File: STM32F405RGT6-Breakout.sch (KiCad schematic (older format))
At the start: 1 part

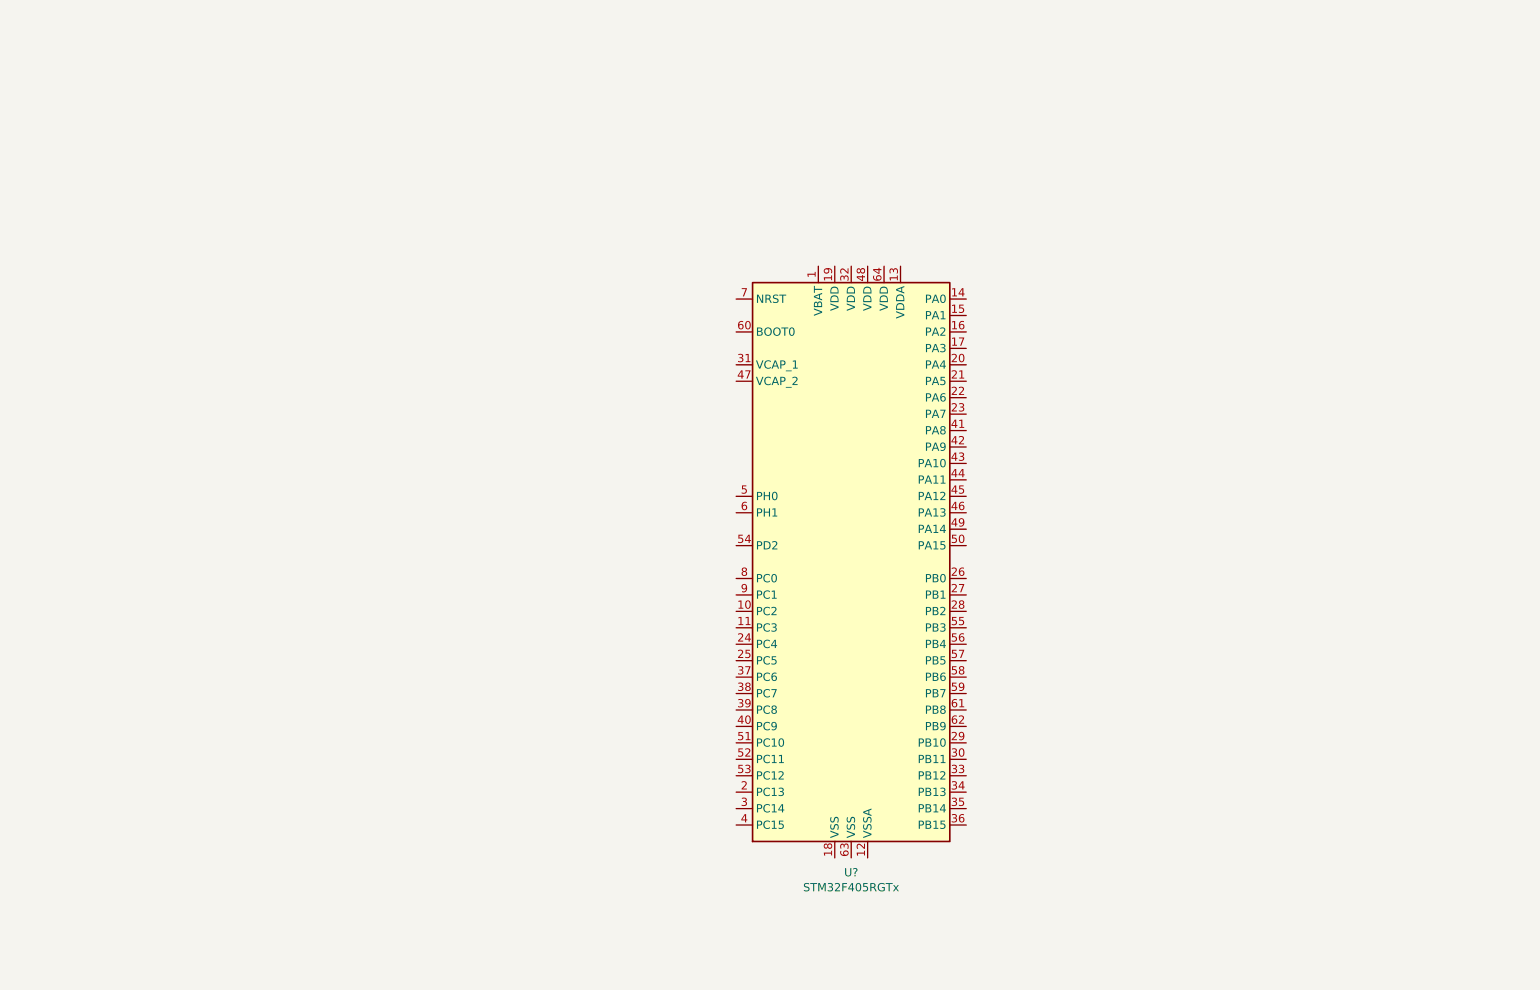
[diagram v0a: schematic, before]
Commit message: Input voltage regulator with pch input reverse polarity protection
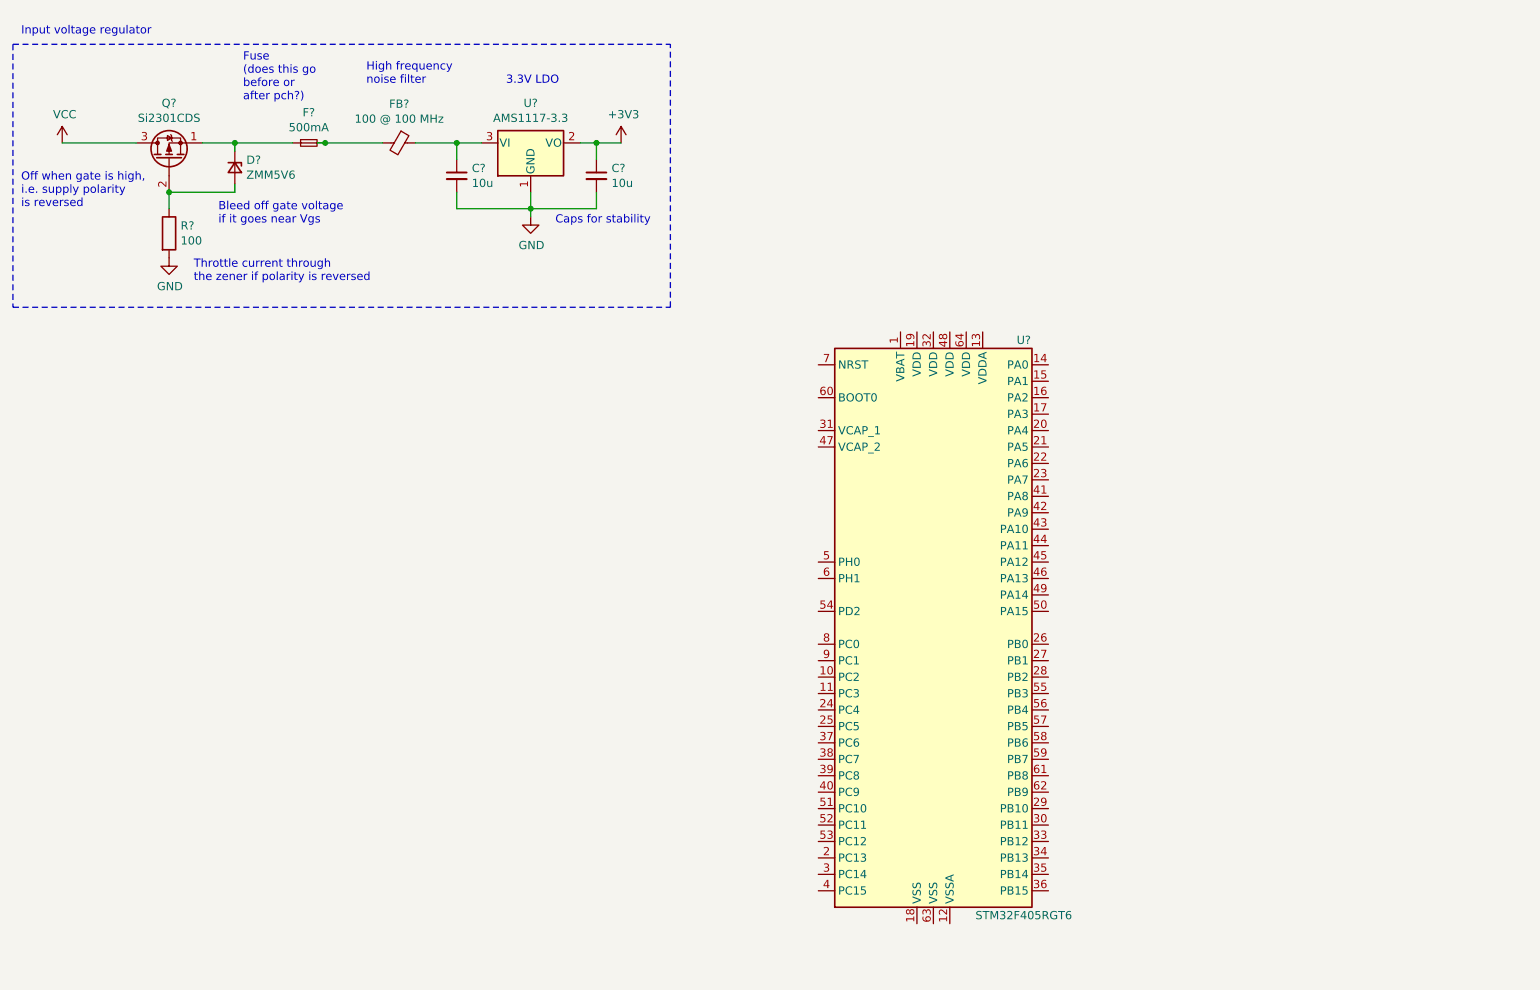
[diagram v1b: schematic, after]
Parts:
- added C? (x2): 10u, symbol Device:C_Small
- added D?: ZMM5V6, symbol Device:D_Zener_Small
- added F?: 500mA, symbol Device:Fuse_Small
- added FB?: 100 @ 100 MHz, symbol Device:Ferrite_Bead_Small
- added Q?: Si2301CDS, symbol Device:Q_PMOS_SGD
- added R?: 100, symbol Device:R
- added U?: AMS1117-3.3, Package_TO_SOT_SMD:SOT-223-3_TabPin2, symbol Regulator_Linear:AMS1117-3.3
- U?: value STM32F405RGTx -> STM32F405RGT6
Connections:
- net labels added: +3V3, GND, VCC
- wire segments 0 -> 21
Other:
- note added: "3.3V LDO"
- note added: "Bleed off gate voltage \nif it goes near Vgs"
- note added: "Caps for stability\n"
- note added: "Fuse\n(does this go \nbefore or \nafter pch?)"
- note added: "High frequency \nnoise filter\n"
- note added: "Input voltage regulator"
- note added: "Off when gate is high,\ni.e. supply polarity \nis reversed"
- note added: "Throttle current through\nthe zener if polarity is reversed\n"
- moved on the sheet: U?
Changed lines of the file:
@@
 L MCU_ST_STM32F4:STM32F405RGTx U?
 U 1 1 61902656
-P 5750 3900
-F 0 "U?" H 5750 2011 50  0000 C CNN
-F 1 "STM32F405RGTx" H 5750 1920 50  0000 C CNN
-F 2 "Package_QFP:LQFP-64_10x10mm_P0.5mm" H 5150 2200 50  0001 R CNN
-F 3 "http://www.st.com/st-web-ui/static/active/en/resource/technical/document/datasheet/DM00037051.pdf" H 5750 3900 50  0001 C CNN
-	1    5750 3900
-	1    0    0    -1
-$EndComp
+P 6250 4300
+F 0 "U?" H 6800 6050 50  0000 C CNN
+F 1 "STM32F405RGT6" H 6800 2550 50  0000 C CNN
+F 2 "Package_QFP:LQFP-64_10x10mm_P0.5mm" H 5650 2600 50  0001 R CNN
+F 3 "http://www.st.com/st-web-ui/static/active/en/resource/technical/document/datasheet/DM00037051.pdf" H 6250 4300 50  0001 C CNN
+	1    6250 4300
+	1    0    0    -1
+$EndComp
+$Comp
+L Regulator_Linear:AMS1117-3.3 U?
+U 1 1 6192F648
+P 3800 1350
+F 0 "U?" H 3800 1592 50  0000 C CNN
+F 1 "AMS1117-3.3" H 3800 1501 50  0000 C CNN
+F 2 "Package_TO_SOT_SMD:SOT-223-3_TabPin2" H 3800 1550 50  0001 C CNN
+F 3 "http://www.advanced-monolithic.com/pdf/ds1117.pdf" H 3900 1100 50  0001 C CNN
+	1    3800 1350
+	1    0    0    -1
+$EndComp
+$Comp
+L Device:Ferrite_Bead_Small FB?
+U 1 1 619351E4
+P 3000 1350
+F 0 "FB?" V 2763 1350 50  0000 C CNN
+F 1 "100 @ 100 MHz" V 2854 1350 50  0000 C CNN
+F 2 "" V 2930 1350 50  0001 C CNN
+F 3 "~" H 3000 1350 50  0001 C CNN
+	1    3000 1350
+	0    1    1    0
+$EndComp
+$Comp
+L Device:Fuse_Small F?
+U 1 1 61935A18
+P 2450 1350
+F 0 "F?" H 2450 1535 50  0000 C CNN
+F 1 "500mA" H 2450 1444 50  0000 C CNN
+F 2 "" H 2450 1350 50  0001 C CNN
+F 3 "~" H 2450 1350 50  0001 C CNN
+	1    2450 1350
+	1    0    0    -1
+$EndComp
+$Comp
+L Device:D_Zener_Small D?
+U 1 1 61943D90
+P 2000 1500
+F 0 "D?" V 1954 1570 50  0000 L CNN
+F 1 "ZMM5V6" V 2045 1570 50  0000 L CNN
+F 2 "" V 2000 1500 50  0001 C CNN
+F 3 "~" V 2000 1500 50  0001 C CNN
+	1    2000 1500
+	0    1    1    0
+$EndComp
+$Comp
+L Device:R R?
+U 1 1 61945077
+P 1600 1900
+F 0 "R?" H 1670 1946 50  0000 L CNN
+F 1 "100" H 1670 1855 50  0000 L CNN
+F 2 "" V 1530 1900 50  0001 C CNN
+F 3 "~" H 1600 1900 50  0001 C CNN
+	1    1600 1900
+	1    0    0    -1
+$EndComp
+Wire Wire Line
+	1600 1650 1600 1750
+Wire Wire Line
+	2000 1650 2000 1600
+Wire Wire Line
+	2000 1400 2000 1350
+Wire Wire Line
+	2500 1350 2550 1350
+Wire Wire Line
+	3100 1350 3350 1350
+$Comp
+L power:GND #PWR?
+U 1 1 6194D181
+P 1600 2050
+F 0 "#PWR?" H 1600 1800 50  0001 C CNN
+F 1 "GND" H 1605 1877 50  0000 C CNN
+F 2 "" H 1600 2050 50  0001 C CNN
+F 3 "" H 1600 2050 50  0001 C CNN
+	1    1600 2050
+	1    0    0    -1
+$EndComp
+$Comp
+L power:VCC #PWR?
+U 1 1 6195256A
+P 950 1350
+F 0 "#PWR?" H 950 1200 50  0001 C CNN
+F 1 "VCC" H 965 1523 50  0000 C CNN
+F 2 "" H 950 1350 50  0001 C CNN
+F 3 "" H 950 1350 50  0001 C CNN
+	1    950  1350
+	1    0    0    -1
+$EndComp
+Wire Wire Line
+	950  1350 1400 1350
+Text Notes 1750 2200 0    50   ~ 0
+Throttle current through\nthe zener if polarity is reversed\n
+Wire Wire Line
+	2000 1350 1800 1350
+Wire Wire Line
+	2000 1350 2350 1350
+Text Notes 1900 1850 0    50   ~ 0
+Bleed off gate voltage \nif it goes near Vgs
+Text Notes 700  1750 0    50   ~ 0
+Off when gate is high,\ni.e. supply polarity \nis reversed
+$Comp
+L power:GND #PWR?
+U 1 1 6194DC8B
+P 3800 1800
+F 0 "#PWR?" H 3800 1550 50  0001 C CNN
+F 1 "GND" H 3805 1627 50  0000 C CNN
+F 2 "" H 3800 1800 50  0001 C CNN
+F 3 "" H 3800 1800 50  0001 C CNN
+	1    3800 1800
+	1    0    0    -1
+$EndComp
+$Comp
+L Device:C_Small C?
+U 1 1 6195B580
+P 3350 1550
+F 0 "C?" H 3442 1596 50  0000 L CNN
+F 1 "10u" H 3442 1505 50  0000 L CNN
+F 2 "" H 3350 1550 50  0001 C CNN
+F 3 "~" H 3350 1550 50  0001 C CNN
+	1    3350 1550
+	1    0    0    -1
+$EndComp
+$Comp
+L Device:C_Small C?
+U 1 1 6195E545
+P 4200 1550
+F 0 "C?" H 4292 1596 50  0000 L CNN
+F 1 "10u" H 4292 1505 50  0000 L CNN
+F 2 "" H 4200 1550 50  0001 C CNN
+F 3 "~" H 4200 1550 50  0001 C CNN
+	1    4200 1550
+	1    0    0    -1
+$EndComp
+Connection ~ 3350 1350
+Wire Wire Line
+	3350 1350 3500 1350
+Wire Wire Line
+	3350 1750 3800 1750
+Wire Wire Line
+	4200 1750 4200 1650
+Connection ~ 3800 1750
+Wire Wire Line
+	3800 1750 4200 1750
+Wire Wire Line
+	3800 1750 3800 1800
+Wire Wire Line
+	4350 1350 4200 1350
+$Comp
+L power:+3V3 #PWR?
+U 1 1 61961ED5
+P 4350 1350
+F 0 "#PWR?" H 4350 1200 50  0001 C CNN
+F 1 "+3V3" H 4365 1523 50  0000 C CNN
+F 2 "" H 4350 1350 50  0001 C CNN
+F 3 "" H 4350 1350 50  0001 C CNN
+	1    4350 1350
+	1    0    0    -1
+$EndComp
+Connection ~ 4200 1350
+Wire Wire Line
+	4200 1350 4100 1350
+Connection ~ 2550 1350
+Wire Wire Line
+	2550 1350 2900 1350
+Text Notes 3950 1850 0    50   ~ 0
+Caps for stability\n
+Text Notes 2800 1000 0    50   ~ 0
+High frequency \nnoise filter\n
+Connection ~ 2000 1350
+$Comp
+L Device:Q_PMOS_SGD Q?
+U 1 1 61942650
+P 1600 1450
+F 0 "Q?" V 1942 1450 50  0000 C CNN
+F 1 "Si2301CDS" V 1851 1450 50  0000 C CNN
+F 2 "" H 1800 1550 50  0001 C CNN
+F 3 "~" H 1600 1450 50  0001 C CNN
+	1    1600 1450
+	0    -1   -1   0
+$EndComp
+Wire Wire Line
+	2000 1650 1600 1650
+Connection ~ 1600 1650
+Text Notes 2050 1100 0    50   ~ 0
+Fuse\n(does this go \nbefore or \nafter pch?)
+Text Notes 3650 1000 0    50   ~ 0
+3.3V LDO
+Wire Wire Line
+	3350 1650 3350 1750
+Wire Wire Line
+	3800 1650 3800 1750
+Wire Wire Line
+	3350 1350 3350 1450
+Wire Wire Line
+	4200 1350 4200 1450
+Wire Notes Line
+	650  750  650  2350
+Wire Notes Line
+	650  2350 4650 2350
+Wire Notes Line
+	4650 2350 4650 750
+Wire Notes Line
+	650  750  4650 750
+Text Notes 700  700  0    50   ~ 0
+Input voltage regulator
 $EndSCHEMATC

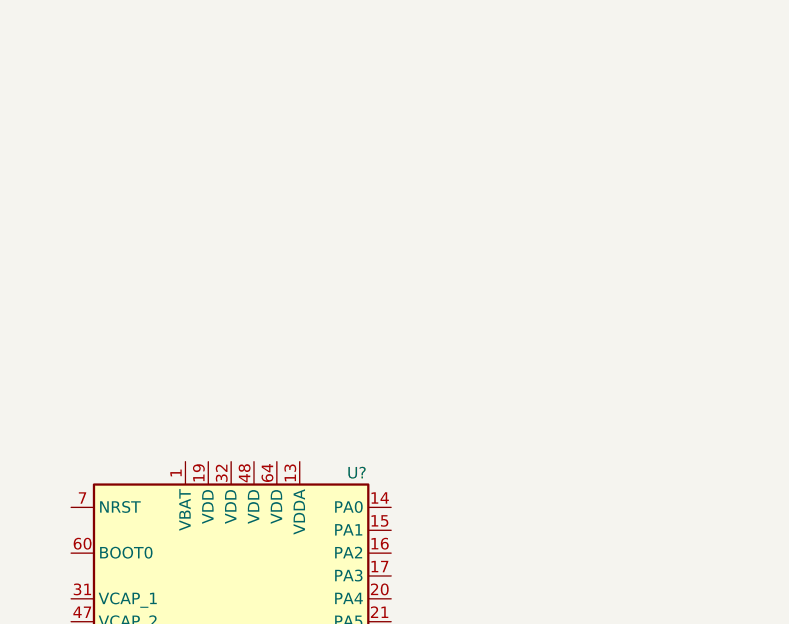
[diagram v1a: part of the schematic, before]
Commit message: ADC voltage reference filter
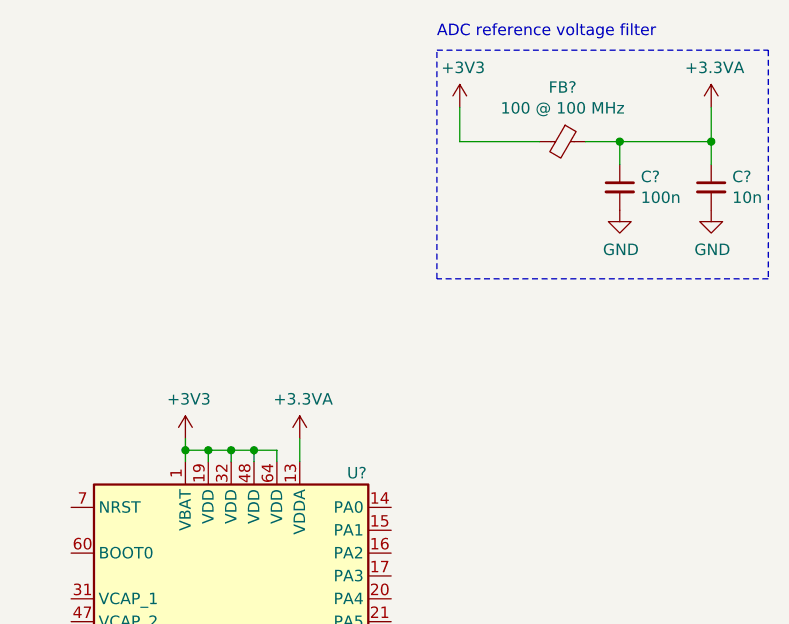
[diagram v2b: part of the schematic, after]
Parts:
- added C?: 100n, symbol Device:C_Small
- added C?: 10n, symbol Device:C_Small
- added FB?: 100 @ 100 MHz, symbol Device:Ferrite_Bead_Small
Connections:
- net labels added: +3.3VA
- wire segments 21 -> 39
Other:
- note added: "ADC reference voltage filter\n"
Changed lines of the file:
@@
 Text Notes 700  700  0    50   ~ 0
 Input voltage regulator
+$Comp
+L power:+3V3 #PWR?
+U 1 1 61974FD8
+P 6050 2400
+F 0 "#PWR?" H 6050 2250 50  0001 C CNN
+F 1 "+3V3" H 6065 2573 50  0000 C CNN
+F 2 "" H 6050 2400 50  0001 C CNN
+F 3 "" H 6050 2400 50  0001 C CNN
+	1    6050 2400
+	1    0    0    -1
+$EndComp
+Wire Wire Line
+	6450 2500 6450 2450
+Wire Wire Line
+	6450 2450 6350 2450
+Wire Wire Line
+	6350 2450 6350 2500
+Wire Wire Line
+	6350 2450 6250 2450
+Wire Wire Line
+	6050 2450 6050 2500
+Connection ~ 6350 2450
+Wire Wire Line
+	6150 2450 6150 2500
+Connection ~ 6150 2450
+Wire Wire Line
+	6150 2450 6050 2450
+Wire Wire Line
+	6250 2450 6250 2500
+Connection ~ 6250 2450
+Wire Wire Line
+	6250 2450 6150 2450
+Wire Wire Line
+	6050 2450 6050 2400
+Connection ~ 6050 2450
+$Comp
+L power:+3V3 #PWR?
+U 1 1 6197E4D1
+P 7250 950
+F 0 "#PWR?" H 7250 800 50  0001 C CNN
+F 1 "+3V3" H 7265 1123 50  0000 C CNN
+F 2 "" H 7250 950 50  0001 C CNN
+F 3 "" H 7250 950 50  0001 C CNN
+	1    7250 950
+	1    0    0    -1
+$EndComp
+$Comp
+L Device:Ferrite_Bead_Small FB?
+U 1 1 6197F29F
+P 7700 1100
+F 0 "FB?" V 7463 1100 50  0000 C CNN
+F 1 "100 @ 100 MHz" V 7554 1100 50  0000 C CNN
+F 2 "" V 7630 1100 50  0001 C CNN
+F 3 "~" H 7700 1100 50  0001 C CNN
+	1    7700 1100
+	0    1    1    0
+$EndComp
+$Comp
+L Device:C_Small C?
+U 1 1 6197FBF2
+P 7950 1300
+F 0 "C?" H 8042 1346 50  0000 L CNN
+F 1 "100n" H 8042 1255 50  0000 L CNN
+F 2 "" H 7950 1300 50  0001 C CNN
+F 3 "~" H 7950 1300 50  0001 C CNN
+	1    7950 1300
+	1    0    0    -1
+$EndComp
+$Comp
+L Device:C_Small C?
+U 1 1 61980239
+P 8350 1300
+F 0 "C?" H 8442 1346 50  0000 L CNN
+F 1 "10n" H 8442 1255 50  0000 L CNN
+F 2 "" H 8350 1300 50  0001 C CNN
+F 3 "~" H 8350 1300 50  0001 C CNN
+	1    8350 1300
+	1    0    0    -1
+$EndComp
+Wire Wire Line
+	8350 1200 8350 1100
+Wire Wire Line
+	8350 1100 7950 1100
+Wire Wire Line
+	7950 1200 7950 1100
+Connection ~ 7950 1100
+Wire Wire Line
+	7950 1100 7800 1100
+Wire Wire Line
+	7250 950  7250 1100
+Wire Wire Line
+	7250 1100 7600 1100
+$Comp
+L power:+3.3VA #PWR?
+U 1 1 61983E43
+P 6550 2400
+F 0 "#PWR?" H 6550 2250 50  0001 C CNN
+F 1 "+3.3VA" H 6565 2573 50  0000 C CNN
+F 2 "" H 6550 2400 50  0001 C CNN
+F 3 "" H 6550 2400 50  0001 C CNN
+	1    6550 2400
+	1    0    0    -1
+$EndComp
+Wire Wire Line
+	6550 2400 6550 2500
+$Comp
+L power:+3.3VA #PWR?
+U 1 1 61985D6F
+P 8350 950
+F 0 "#PWR?" H 8350 800 50  0001 C CNN
+F 1 "+3.3VA" H 8365 1123 50  0000 C CNN
+F 2 "" H 8350 950 50  0001 C CNN
+F 3 "" H 8350 950 50  0001 C CNN
+	1    8350 950
+	1    0    0    -1
+$EndComp
+Wire Wire Line
+	8350 950  8350 1100
+Connection ~ 8350 1100
+$Comp
+L power:GND #PWR?
+U 1 1 6198711A
+P 7950 1400
+F 0 "#PWR?" H 7950 1150 50  0001 C CNN
+F 1 "GND" H 7955 1227 50  0000 C CNN
+F 2 "" H 7950 1400 50  0001 C CNN
+F 3 "" H 7950 1400 50  0001 C CNN
+	1    7950 1400
+	1    0    0    -1
+$EndComp
+$Comp
+L power:GND #PWR?
+U 1 1 61987910
+P 8350 1400
+F 0 "#PWR?" H 8350 1150 50  0001 C CNN
+F 1 "GND" H 8355 1227 50  0000 C CNN
+F 2 "" H 8350 1400 50  0001 C CNN
+F 3 "" H 8350 1400 50  0001 C CNN
+	1    8350 1400
+	1    0    0    -1
+$EndComp
+Wire Notes Line
+	8600 700  8600 1700
+Wire Notes Line
+	8600 1700 7150 1700
+Wire Notes Line
+	7150 1700 7150 700
+Wire Notes Line
+	7150 700  8600 700
+Text Notes 7150 650  0    50   ~ 0
+ADC reference voltage filter\n
 $EndSCHEMATC

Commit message: decoupling
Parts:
- added C? (x8): 100u, symbol Device:C_Small
- added C?: 10u, symbol Device:C_Small
- added C? (x2): 2.2u, symbol Device:C_Small
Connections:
- net +3V3: now also C?.1, C?.1, C?.1, C?.1, C?.1, C?.1, C?.1, C?.1, C?.1
- net GND: now also C?.2, C?.2, C?.2, C?.2, C?.2, C?.2, C?.2, C?.2, C?.2, C?.2, C?.2
- net at U?.31 (VCAP_1): now also C?.1
- net at U?.47 (VCAP_2): now also C?.1
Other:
- note added: "Decoupling: 2x100u per VDD + 10u bulk close to chip"
- note added: "Internal\nvoltage\nregulator\nfiltering"
- moved on the sheet: C?, FB?

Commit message: boot mode pins
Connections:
- net BOOT1: now reaches U?.28 (PB2)
- net BOOT0: now reaches U?.60 (BOOT0)
- net NRST: now reaches U?.7 (NRST)
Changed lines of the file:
@@
 Text Notes 4550 3600 0    50   ~ 0
 Internal\nvoltage\nregulator\nfiltering
+Text GLabel 5550 2700 0    50   Input ~ 0
+NRST
+Text GLabel 5550 2900 0    50   Input ~ 0
+BOOT0
+Text GLabel 6950 4600 2    50   Input ~ 0
+BOOT1
 $EndSCHEMATC

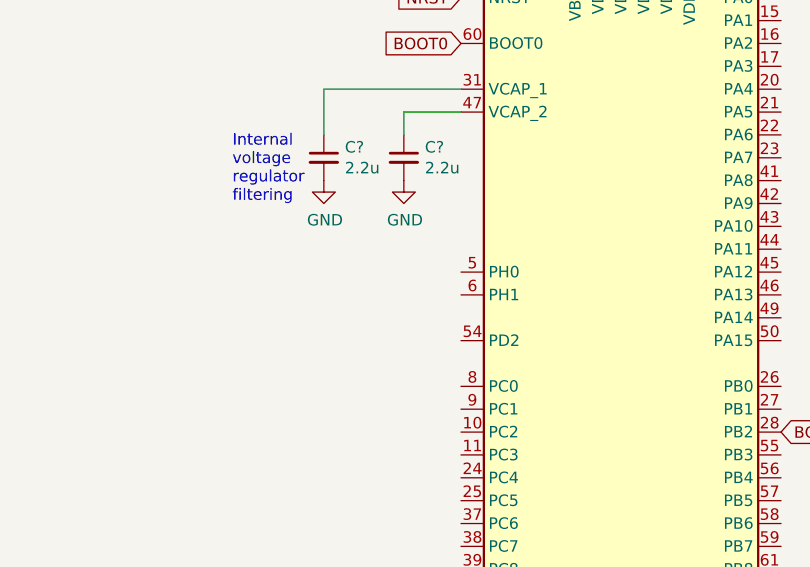
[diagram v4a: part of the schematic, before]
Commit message: Configure pins for high speed crystal
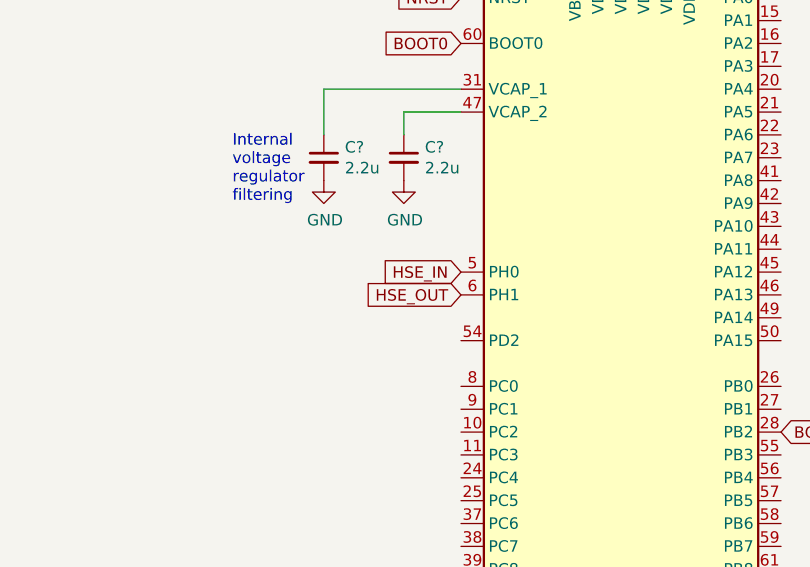
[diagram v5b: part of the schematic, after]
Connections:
- net HSE_IN: now reaches U?.5 (PH0)
- net HSE_OUT: now reaches U?.6 (PH1)
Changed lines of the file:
@@
 Text GLabel 6950 4600 2    50   Input ~ 0
 BOOT1
+Text GLabel 5550 3900 0    50   Input ~ 0
+HSE_IN
+Text GLabel 5550 4000 0    50   Input ~ 0
+HSE_OUT
 $EndSCHEMATC
